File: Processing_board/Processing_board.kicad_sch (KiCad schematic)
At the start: 19 parts, among them IC1 THS4031IDGNR, J1 USB_C_Receptacle_USB2.0_16P, U1 STM32WBA63CIU6, U2 ADS7953SBDBT, U3 MCP2210x-SO, U4 REF5025ID

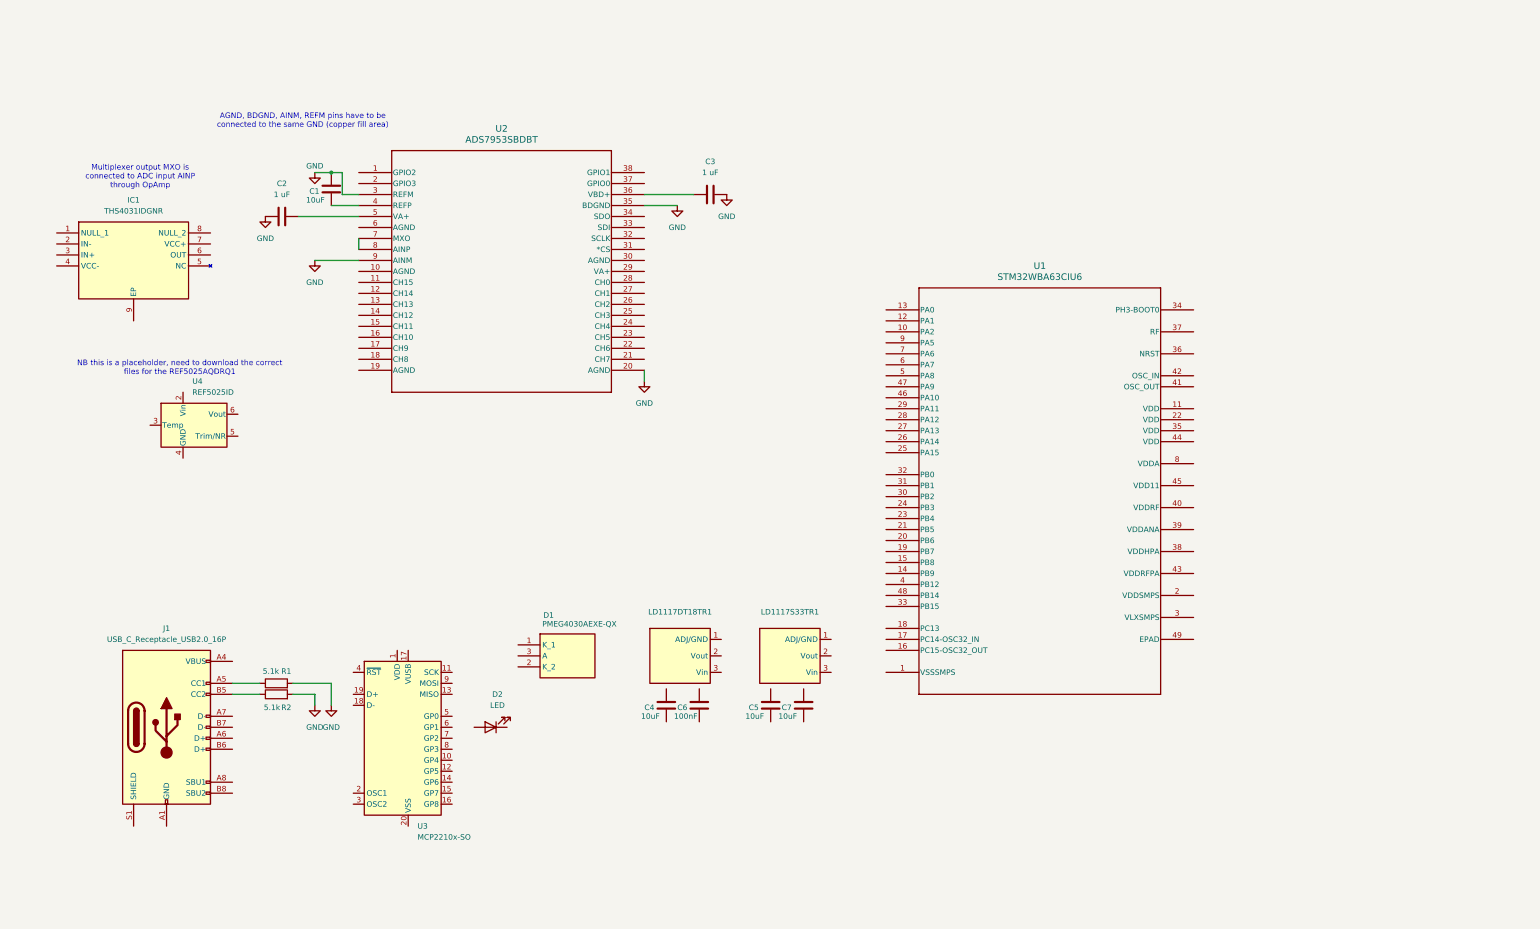
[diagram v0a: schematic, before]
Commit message: first version of circuit schematic of signal processing board
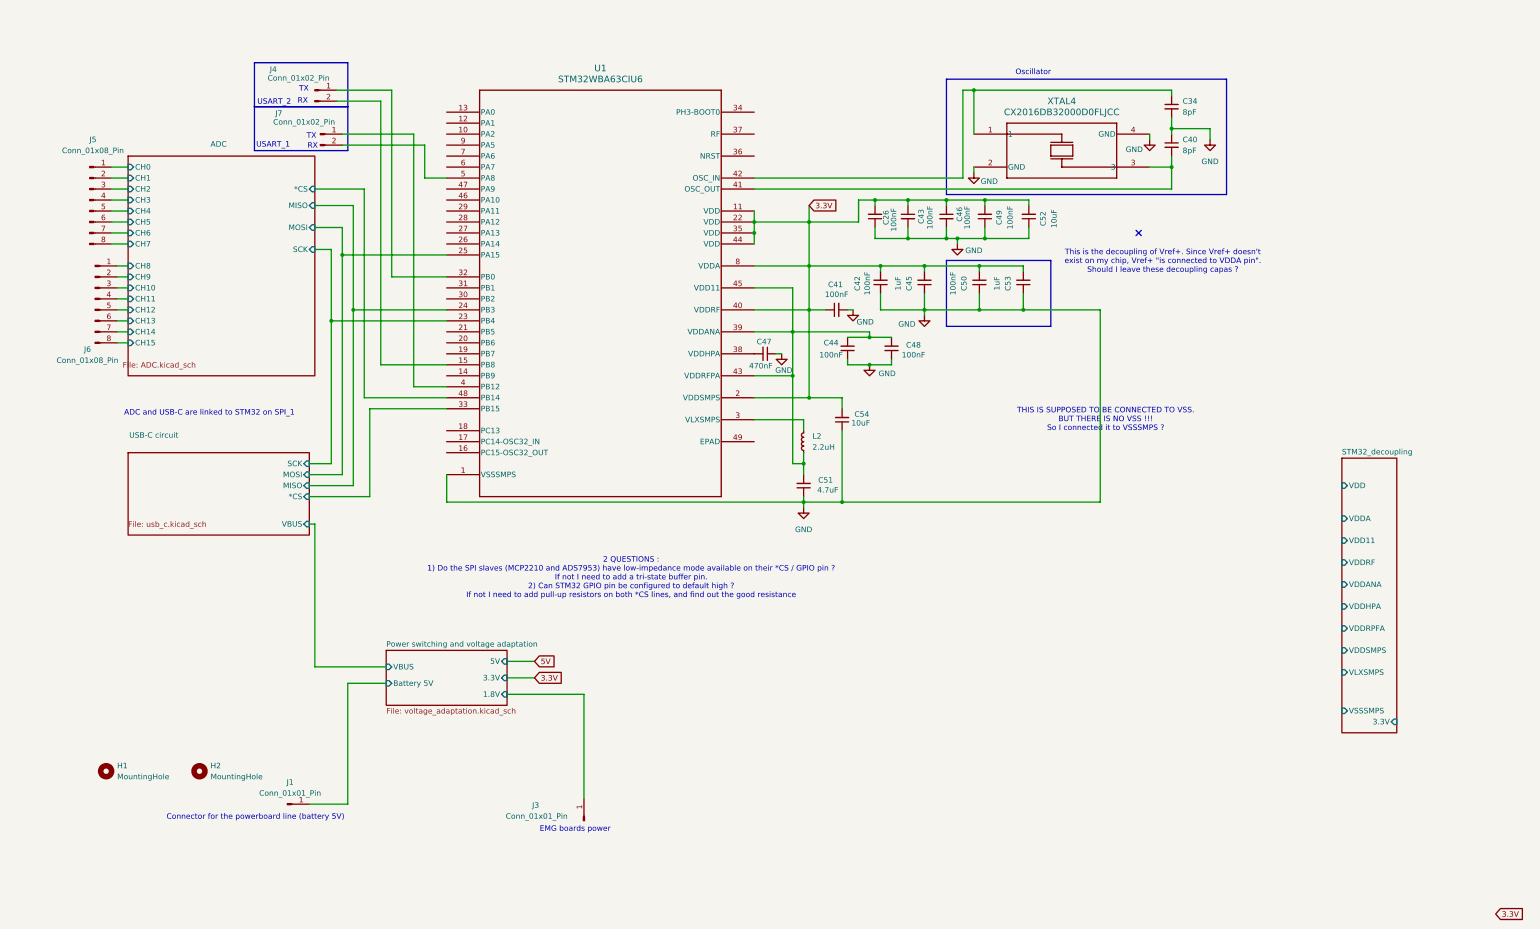
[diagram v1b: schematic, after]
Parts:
- removed C1, C4, C5, C7: 10uF, symbol Device:C
- removed C2, C3: 1 uF, symbol Device:C
- removed C6: 100nF, symbol Device:C
- removed D1: PMEG4030AEXE-QX, PMEG4030AEXEQX, symbol PMEG4030AEXE-QX:PMEG4030AEXE-QX
- removed D2: LED, symbol Device:LED
- removed IC1: THS4031IDGNR, SOP65P490X110-9N, symbol THS4031IDGNR:THS4031IDGNR
- removed J1: USB_C_Receptacle_USB2.0_16P, symbol Connector:USB_C_Receptacle_USB2.0_16P
- removed LD1117DT18TR1: ~, symbol Custom_Symbol_Library_Npulse:LD1117DT18TR
- removed LD1117S33TR1: ~, symbol Custom_Symbol_Library_Npulse:LD1117S33TR (pack SOT-223)
- removed R1, R2: 5.1k, symbol Device:R
- removed U2: ADS7953SBDBT, DBT38, symbol 2025-03-12_09-53-19:ADS7953SBDBT
- removed U3: MCP2210x-SO, Package_SO:SOIC-20W_7.5x12.8mm_P1.27mm, symbol Interface_USB:MCP2210x-SO
- removed U4: REF5025ID, Package_SO:SOIC-8_3.9x4.9mm_P1.27mm, symbol Reference_Voltage:REF5025ID
- added C26, C41, C42, C43, C44, C46, C48, C49, C50: 100nF, symbol Device:C_Small
- added C34, C40: 8pF, symbol Device:C_Small
- added C45, C53: 1uF, symbol Device:C_Small
- added C47: 470nF, symbol Device:C_Small
- added C51: 4.7uF, symbol Device:C_Small
- added C52, C54: 10uF, symbol Device:C_Small
- added H1, H2: MountingHole, symbol Mechanical:MountingHole
- added J1, J3: Conn_01x01_Pin, symbol Connector:Conn_01x01_Pin
- added J4, J7: Conn_01x02_Pin, symbol Connector:Conn_01x02_Pin
- added J5, J6: Conn_01x08_Pin, symbol Connector:Conn_01x08_Pin
- added L2: 2.2uH, symbol Device:L_Small
- added XTAL4: CX2016DB32000D0FLJCC, xtal4_CX2016DB_AVX, symbol CX2016DB32000D0FLJCC:CX2016DB32000D0FLJCC
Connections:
- net GND: now also U1.1 (VSSSMPS), C26.1, C34.2, C40.1, C41.2, C42.1, C43.2, C44.1, C45.1, C46.2, C47.1, C48.1, C49.1, C50.1, C51.1, C52.1, C53.1, C54.1, XTAL4.2 (GND), XTAL4.4 (GND)
- net 3.3V: now reaches U1.11 (VDD)
- net 3.3V: now also U1.2 (VDDSMPS), U1.22 (VDD), U1.35 (VDD), U1.40 (VDDRF), U1.44 (VDD), U1.8 (VDDA), C26.2, C41.1, C42.2, C43.1, C45.2, C46.1, C49.2, C50.2, C52.2, C53.2, C54.2
- net at U1.15 (PB8): now also J4.2 (Pin_2)
- net ADC/SCK: now reaches U1.23 (PB4)
- net ADC/MISO: now reaches U1.24 (PB3)
- net ADC/MOSI: now reaches U1.25 (PA15)
- net at U1.3 (VLXSMPS): now also L2.2
- net at U1.32 (PB0): now also J4.1 (Pin_1)
- net USB-C circuit/*CS: now reaches U1.33 (PB15)
- net at U1.38 (VDDHPA): now also C47.2
- net at U1.39 (VDDANA): now also U1.43 (VDDRFPA), U1.45 (VDD11), C44.2, C48.2, C51.2, L2.1
- net at U1.4 (PB12): now also J7.1 (Pin_1)
- net at U1.41 (OSC_OUT): now also C40.2, XTAL4.3
- net at U1.42 (OSC_IN): now also C34.1, XTAL4.1
- net ADC/*CS: now reaches U1.48 (PB14)
- net at U1.5 (PA8): now also J7.2 (Pin_2)
- new net ADC/CH0: J5.1 (Pin_1)
- new net ADC/CH1: J5.2 (Pin_2)
- new net ADC/CH10: J6.3 (Pin_3)
- new net ADC/CH11: J6.4 (Pin_4)
- new net ADC/CH12: J6.5 (Pin_5)
- new net ADC/CH13: J6.6 (Pin_6)
- new net ADC/CH14: J6.7 (Pin_7)
- new net ADC/CH15: J6.8 (Pin_8)
- new net ADC/CH2: J5.3 (Pin_3)
- new net ADC/CH3: J5.4 (Pin_4)
- new net ADC/CH4: J5.5 (Pin_5)
- new net ADC/CH5: J5.6 (Pin_6)
- new net ADC/CH6: J5.7 (Pin_7)
- new net ADC/CH7: J5.8 (Pin_8)
- new net ADC/CH8: J6.1 (Pin_1)
- new net ADC/CH9: J6.2 (Pin_2)
- new net Power switching and voltage adaptation/1.8V: J3.1 (Pin_1)
- new net Power switching and voltage adaptation/Battery 5V: J1.1 (Pin_1)
- no-connect marks 0 -> 1
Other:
- added sheet ADC (ADC.kicad_sch)
- added sheet Power switching and voltage adaptation (voltage_adaptation.kicad_sch)
- added sheet STM32_decoupling (STM32_decoupling.kicad_sch)
- added sheet USB-C circuit (usb_c.kicad_sch)
- note added: "2 QUESTIONS : 1) Do the SPI slaves (MCP2210 and ADS7953) have low-impedance mode available on their *CS / GPIO pin ? If not I need to add a tri-state buffer pin. 2) Can STM32 GPIO pin be configured to default high ? If not I need to add pull-up resistors on both *CS lines, and find out the good resistance"
- note added: "ADC and USB-C are linked to STM32 on SPI_1"
- note added: "Connector for the powerboard line (battery 5V)"
- note added: "EMG boards power"
- note added: "Oscillator"
- note added: "RX"
- note added: "THIS IS SUPPOSED TO BE CONNECTED TO VSS. BUT THERE IS NO VSS !!! So I connected it to VSSSMPS ?"
- note added: "TX"
- note added: "This is the decoupling of Vref+. Since Vref+ doesn't exist on my chip, Vref+ "is connected to VDDA pin". Should I leave these decoupling capas ?"
- note added: "USART_1"
- note added: "USART_2"
- note removed: "AGND, BDGND, AINM, REFM pins have to be connected to the same GND (copper fill area)"
- note removed: "Multiplexer output MXO is connected to ADC input AINP through OpAmp"
- note removed: "NB this is a placeholder, need to download the correct files for the REF5025AQDRQ1"
- moved on the sheet: U1

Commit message: the 2nd (hopefully final) version of circuit diagram
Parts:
- removed C26, C41, C42, C43, C44, C46, C48, C49, C50: 100nF, symbol Device:C_Small
- removed C45, C53: 1uF, symbol Device:C_Small
- removed C47: 470nF, symbol Device:C_Small
- removed C51: 4.7uF, symbol Device:C_Small
- removed C52, C54: 10uF, symbol Device:C_Small
- removed L2: 2.2uH, symbol Device:L_Small
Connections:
- net 3.3V: no longer U1.11 (VDD), U1.2 (VDDSMPS), U1.22 (VDD), U1.35 (VDD), U1.40 (VDDRF), U1.44 (VDD), U1.8 (VDDA)
- net GND: no longer U1.1 (VSSSMPS)
- net STM32_power_supply_scheme/VDD: now also U1.11 (VDD), U1.22 (VDD), U1.35 (VDD), U1.44 (VDD)
- net STM32_power_supply_scheme/VDD11: now also U1.45 (VDD11)
- net STM32_power_supply_scheme/VDDA: now also U1.8 (VDDA)
- net STM32_power_supply_scheme/VDDANA: now also U1.39 (VDDANA)
- net STM32_power_supply_scheme/VDDHPA: now also U1.38 (VDDHPA)
- net STM32_power_supply_scheme/VDDRF: now also U1.40 (VDDRF)
- net STM32_power_supply_scheme/VDDRPFA: now also U1.43 (VDDRFPA)
- net STM32_power_supply_scheme/VDDSMPS: now also U1.2 (VDDSMPS)
- net STM32_power_supply_scheme/VLXSMPS: now also U1.3 (VLXSMPS)
- net STM32_power_supply_scheme/VSSSMPS: now also U1.1 (VSSSMPS)
- net STM32_power_supply_scheme/VSS: now reaches U1.49 (EPAD)
- no-connect marks 1 -> 0
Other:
- sheet STM32_decoupling renamed STM32_power_supply_scheme
- sheet STM32_power_supply_scheme: file STM32_decoupling.kicad_sch -> STM32_power_supply_scheme.kicad_sch
- sheet STM32_power_supply_scheme ports: added VSS; removed 3.3V
- note added: "1 QUESTION : 1) Do the SPI slaves (MCP2210 and ADS7953) have low-impedance mode available on their *CS / GPIO pin ? If not I need to add a tri-state buffer pin."
- note removed: "2 QUESTIONS : 1) Do the SPI slaves (MCP2210 and ADS7953) have low-impedance mode available on their *CS / GPIO pin ? If not I need to add a tri-state buffer pin. 2) Can STM32 GPIO pin be configured to default high ? If not I need to add pull-up resistors on both *CS lines, and find out the good resistance"
- note removed: "THIS IS SUPPOSED TO BE CONNECTED TO VSS. BUT THERE IS NO VSS !!! So I connected it to VSSSMPS ?"
- note removed: "This is the decoupling of Vref+. Since Vref+ doesn't exist on my chip, Vref+ "is connected to VDDA pin". Should I leave these decoupling capas ?"

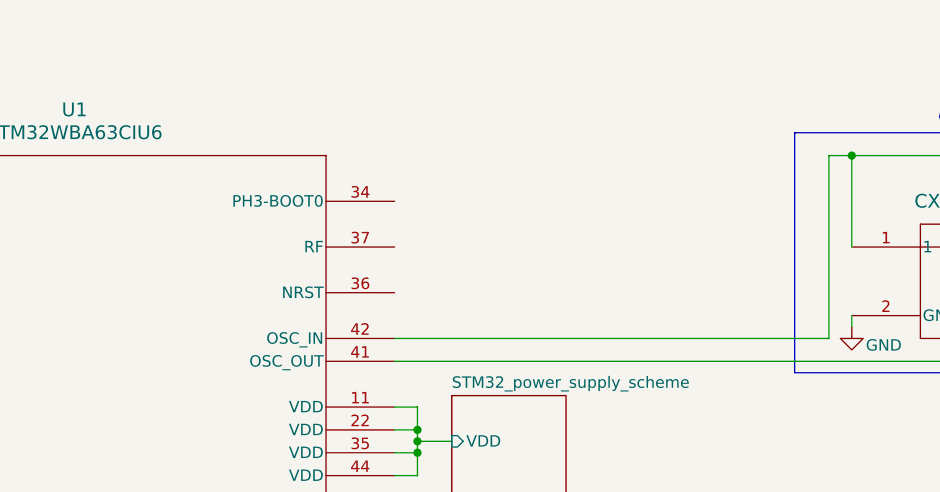
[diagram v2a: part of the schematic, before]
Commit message: added reset button
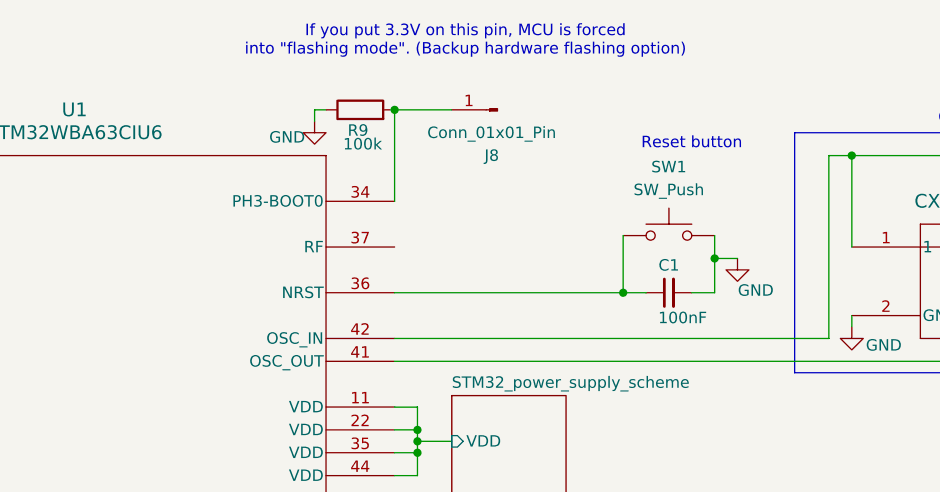
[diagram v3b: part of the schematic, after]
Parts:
- added C1: 100nF, symbol Device:C_Small
- added J8: Conn_01x01_Pin, symbol Connector:Conn_01x01_Pin
- added R9: 100k, symbol Device:R
- added SW1: SW_Push, symbol Switch:SW_Push
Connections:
- net GND: now also C1.2, R9.1, SW1.2
- net at U1.34 (PH3-BOOT0): now also J8.1 (Pin_1), R9.2
- net at U1.36 (NRST): now also C1.1, SW1.1
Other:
- note added: "If you put 3.3V on this pin, MCU is forced into "flashing mode". (Backup hardware flashing option)"
- note added: "Reset button"
- company: (none) -> N-Pulse
- title: (none) -> EMG signal processing board

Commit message: addressed all reviews except the LDO 5V
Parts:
- removed J1, J3, J8: Conn_01x01_Pin, symbol Connector:Conn_01x01_Pin
- added C3: 100nF, symbol Device:C_Small
- added D8: IN_S42BT LED, symbol Device:LED
- added J1: Conn_01x06_Pin, symbol Connector:Conn_01x06_Pin
- added J10, J9: Conn_01x03_Pin, symbol Connector:Conn_01x03_Pin
- added R12, R13: 100R, symbol Device:R
- added SW2: SW_Push, symbol Switch:SW_Push
- R9: value 100k -> 10k
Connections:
- net 3.3V: now also J1.2 (Pin_2), SW2.1
- net GND: now also J4.2 (Pin_2), J7.1 (Pin_1), C3.1, J1.1 (Pin_1), J10.1 (Pin_1), J9.1 (Pin_1)
- net Battery 5V: now reaches J4.1 (Pin_1)
- net Battery 5V: no longer U1.32 (PB0)
- net SPI3_MOSI: now reaches U1.15 (PB8)
- net SPI3_MOSI: no longer J4.2 (Pin_2)
- net SPI3_SCK: now reaches U1.13 (PA0)
- net SWCLK: now reaches U1.26 (PA14)
- net SWCLK: now also J1.5 (Pin_5)
- net SWDIO: now reaches U1.27 (PA13)
- net SWDIO: now also J1.4 (Pin_4)
- net ADC/GPIO3: now reaches U1.30 (PB2)
- net ADC/GPIO2: now reaches U1.31 (PB1)
- net BOOT0: now reaches R9.2, U1.34 (PH3-BOOT0)
- net BOOT0: now also C3.2, R12.1
- net SWD_NRST: now reaches C1.1, SW1.1
- net SWD_NRST: now also J1.3 (Pin_3), R13.1; no longer U1.36 (NRST)
- net USART1_TX: now reaches U1.4 (PB12)
- net USART1_TX: no longer J7.1 (Pin_1)
- net ADC *CS: now reaches U1.46 (PA10)
- net SPI3_MISO: now reaches U1.47 (PA9)
- net EMG_modules_1.8V: now reaches J7.2 (Pin_2)
- net EMG_modules_1.8V: no longer U1.5 (PA8)
- net at U1.6 (PA7): now also J9.3 (Pin_3)
- net at U1.9 (PA5): now also J9.2 (Pin_2)
- net ADC/*CS: no longer names the net of U1.48 (PB14)
- net ADC/MISO renamed Traces
- net Traces: now also J1.6 (Pin_6)
- net ADC/MOSI: no longer names the net of U1.25 (PA15)
- net ADC/SCK renamed USART2_RX
- net USART2_RX: now also J10.3 (Pin_3)
- net USB-C circuit/*CS renamed LED
- net LED: now also D8.2 (A)
- new net: R12.2, SW2.2
- new net: R13.2, U1.36 (NRST)
- new net USART1_RX: U1.5 (PA8)
- new net USART2_TX: J10.2 (Pin_2), U1.32 (PB0)
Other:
- sheet ADC ports: added GPIO2, GPIO3; removed none
- sheet USB-C circuit ports: added RX, TX; removed *CS, MISO, MOSI, SCK
- note added: "ADC is linked to STM32 on SPI_3 MCP2220 is linked to STM32 on USART1"
- note added: "CL = (Cl1*Cl2)/(Cl1+Cl2) + Cs CL = crystal's load capacitance Cs = stray capacitance (assumed 4pF) Cl1= Cl2 = pierce oscillator's capacitors Cl"
- note added: "Cl = 2(CL-Cs) = 2(8-4) = 8 pF"
- note added: "NRST"
- note added: "Push and maintain button BEFORE board power-up (or reset) to enter flashing mode"
- note added: "QUESTIONS : 1) Each LED consumes ~10mA. Is that too much ? 2) How much current do I actually have available ? 3) I feel like my power switching/voltage adaptation circuit is shit"
- note added: "R12 and C3 in combo with the pulldown resistor form a low-pass filter for button debouncing"
- note added: "SPI3_MOSI"
- note added: "SPI3_SCK"
- note added: "SWCLK"
- note added: "SWD traces"
- note added: "SWD/JTAG"
- note added: "SWD/JTAG is for debug and flashing (apparently UART can also be used for flashing ?) IO & CLK are important, Trace is for additional debug capability or can be GPIO if needed"
- note added: "SWDIO"
- note added: "Traces"
- note added: "USART2 RX"
- note added: "USART3 TX"
- note added: "USART3_RX"
- note added: "USART_1 RX"
- note added: "USART_1 TX"
- note added: "USART_2 TX"
- note added: "USART_3"
- note removed: "1 QUESTION : 1) Do the SPI slaves (MCP2210 and ADS7953) have low-impedance mode available on their *CS / GPIO pin ? If not I need to add a tri-state buffer pin."
- note removed: "ADC and USB-C are linked to STM32 on SPI_1"
- note removed: "If you put 3.3V on this pin, MCU is forced into "flashing mode". (Backup hardware flashing option)"
- note removed: "USART_1"
- moved on the sheet: C1, C34, C40, H1, H2, J5, J6, R9, SW1, U1, XTAL4

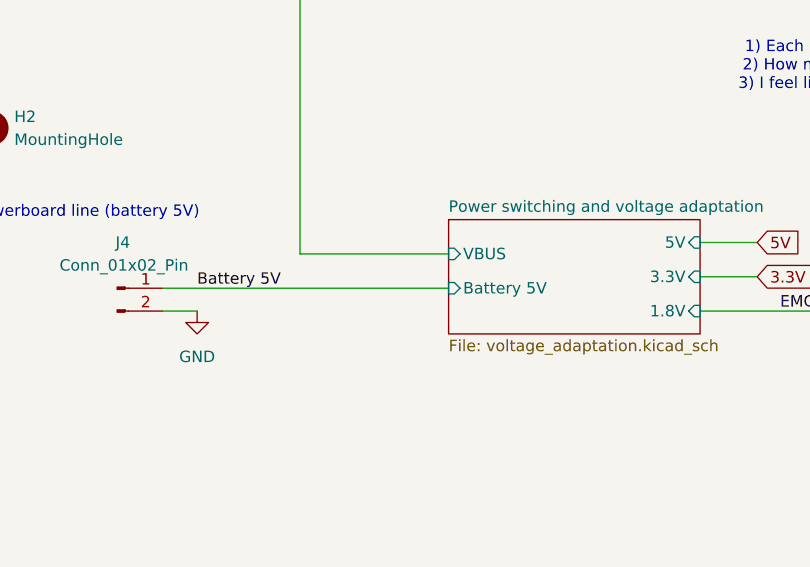
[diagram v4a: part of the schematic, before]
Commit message: 5V LDO and jumper cables to handle 2S battery OR johann's powerline
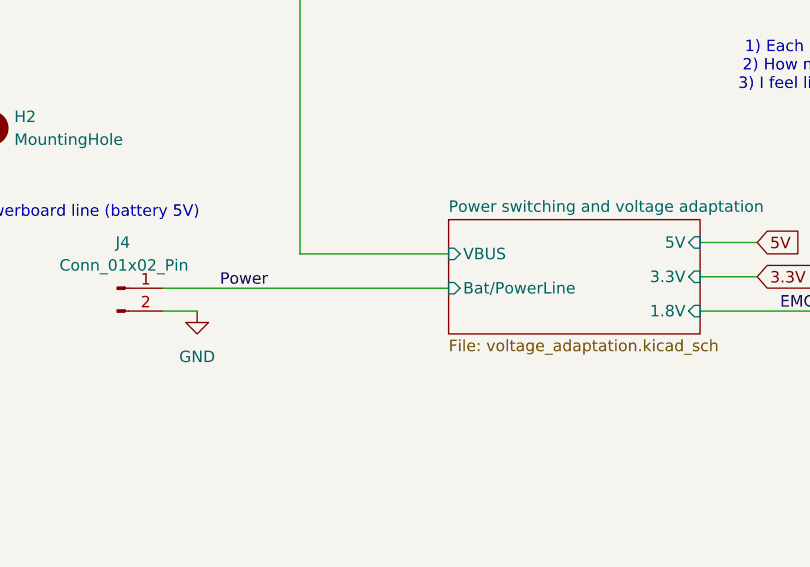
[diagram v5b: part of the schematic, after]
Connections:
- net Battery 5V renamed Power
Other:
- sheet Power switching and voltage adaptation ports: added Bat/PowerLine; removed Battery 5V
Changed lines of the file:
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@@
 		)
 	)
-	(label "Battery 5V"
-		(at 60.96 176.53 0)
+	(label "Power"
+		(at 63.5 176.53 0)
 		(effects
 			(font
@@
 			)
 		)
-		(pin "Battery 5V" input
-			(at 88.9 176.53 180)
-			(effects
-				(font
-					(size 1.27 1.27)
-				)
-				(justify left)
-			)
-		)
 		(pin "VBUS" input
 			(at 88.9 172.72 180)
@@
 			)
 		)
+		(pin "Bat{slash}PowerLine" input
+			(at 88.9 176.53 180)
+			(effects
+				(font
+					(size 1.27 1.27)
+				)
+				(justify left)
+			)
+		)
